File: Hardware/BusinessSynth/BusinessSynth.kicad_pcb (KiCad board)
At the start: 2 copper layers, 96 x 55 mm, 71 parts, among them J1 StylusKey, J2 StylusKey, J3 StylusKey, J4 StylusKey, J5 StylusKey, J6 StylusKey, J7 StylusKey, J8 StylusKey, J9 StylusKey, Q1 Q_PNP_BEC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

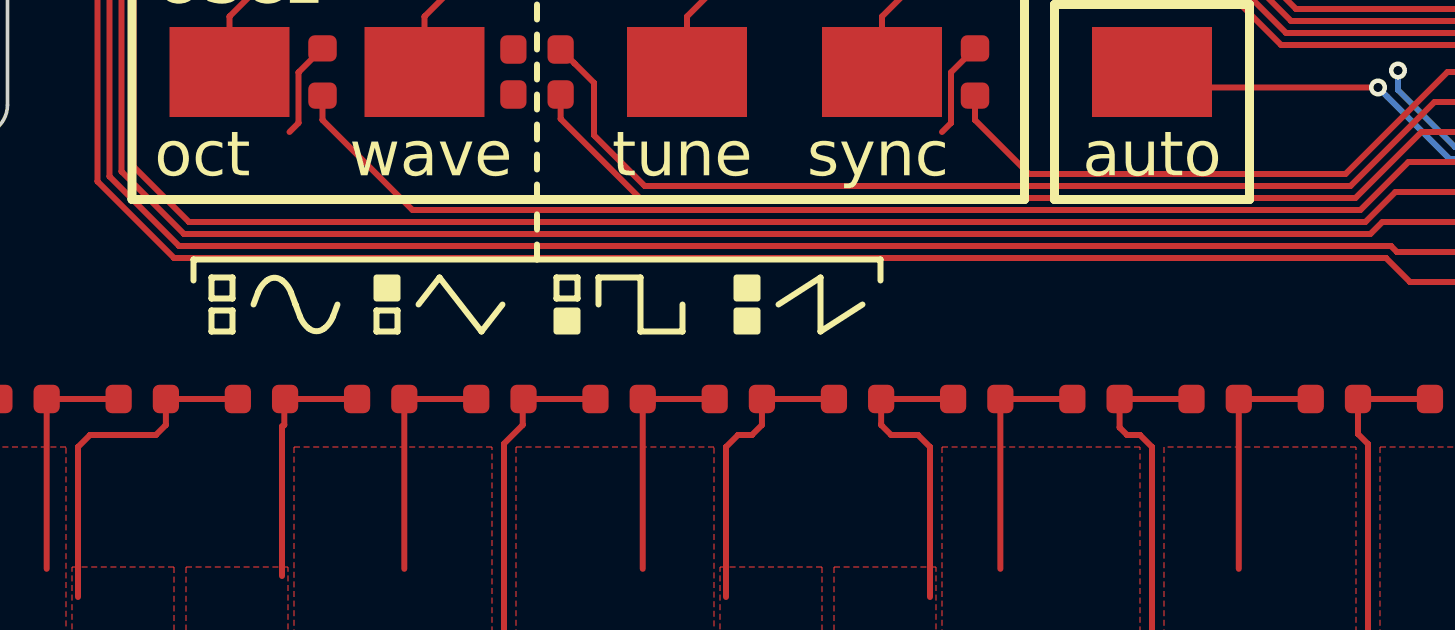
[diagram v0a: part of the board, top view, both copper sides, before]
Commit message: Add glide functionality to oscillator
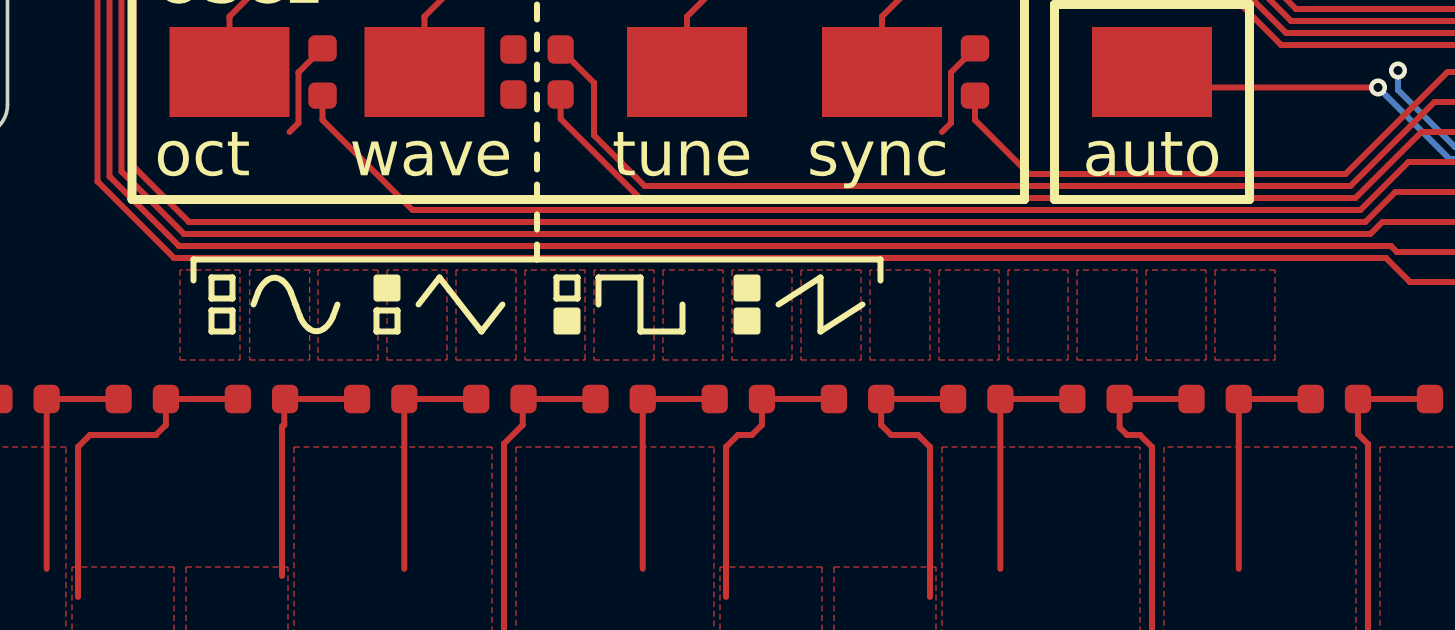
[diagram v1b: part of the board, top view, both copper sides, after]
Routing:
- added copper zone on F.Cu, net (none)
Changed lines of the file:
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@@
-(kicad_pcb (version 20171130) (host pcbnew "(5.1.0)-1")
+(kicad_pcb (version 20171130) (host pcbnew "(5.1.2)-2")
   (general
     (thickness 0.6)
-    (drawings 127)
+    (drawings 128)
     (tracks 352)
     (zones 0)
@@
   (layers
     (0 F.Cu signal)
-    (31 B.Cu signal)
-    (32 B.Adhes user)
-    (33 F.Adhes user)
-    (34 B.Paste user)
-    (35 F.Paste user)
-    (36 B.SilkS user)
-    (37 F.SilkS user)
-    (38 B.Mask user)
+    (31 B.Cu signal hide)
+    (32 B.Adhes user hide)
+    (33 F.Adhes user hide)
+    (34 B.Paste user hide)
+    (35 F.Paste user hide)
+    (36 B.SilkS user hide)
+    (37 F.SilkS user hide)
+    (38 B.Mask user hide)
     (39 F.Mask user)
-    (40 Dwgs.User user)
-    (41 Cmts.User user)
-    (42 Eco1.User user)
-    (43 Eco2.User user)
-    (44 Edge.Cuts user)
-    (45 Margin user)
+    (40 Dwgs.User user hide)
+    (41 Cmts.User user hide)
+    (42 Eco1.User user hide)
+    (43 Eco2.User user hide)
+    (44 Edge.Cuts user hide)
+    (45 Margin user hide)
     (46 B.CrtYd user hide)
     (47 F.CrtYd user hide)
@@
       (net 1 GND) (zone_connect 1) (thermal_gap 0.3))
   )
+  (dimension 3.001666 (width 0.12) (layer F.SilkS)
+    (gr_text "3.002 mm" (at 139.077487 96.545751 -88.09084757) (layer F.SilkS)
+      (effects (font (size 1 1) (thickness 0.15)))
+    )
+    (feature1 (pts (xy 140.4 95) (xy 139.710687 95.022977)))
+    (feature2 (pts (xy 140.5 98) (xy 139.810687 98.022977)))
+    (crossbar (pts (xy 140.396782 98.003441) (xy 140.296782 95.003441)))
+    (arrow1a (pts (xy 140.296782 95.003441) (xy 140.920407 96.109783)))
+    (arrow1b (pts (xy 140.296782 95.003441) (xy 139.748216 96.148856)))
+    (arrow2a (pts (xy 140.396782 98.003441) (xy 140.945348 96.858026)))
+    (arrow2b (pts (xy 140.396782 98.003441) (xy 139.773157 96.897099)))
+  )
   (gr_line (start 132.35 104.45) (end 131.65 104.45) (layer F.SilkS) (width 0.2))
   (gr_line (start 131.65 105.15) (end 132.35 105.15) (layer F.SilkS) (width 0.2))
@@
   (gr_line (start 102 125) (end 188 125) (layer Edge.Cuts) (width 0.15))
   (gr_line (start 100 72) (end 100 123) (layer Edge.Cuts) (width 0.15))
-  (via (at 178.262742 84.5) (size 0.8) (drill 0.4) (layers F.Cu B.Cu) (net 30))
-  (segment (start 179.38873 83.374012) (end 178.262742 84.5) (width 0.5) (layer B.Cu) (net 30))
   (via (at 193.5 120.75) (size 0.6) (drill 0.3) (layers F.Cu B.Cu) (net 1))
   (via (at 103.25 107.4) (size 0.6) (drill 0.3) (layers F.Cu B.Cu) (net 1))
@@
   (segment (start 169.535 88.465) (end 169 88.465) (width 0.2) (layer F.Cu) (net 29))
   (segment (start 169.735 88.265) (end 169.535 88.465) (width 0.2) (layer F.Cu) (net 29))
+  (via (at 178.262742 84.5) (size 0.8) (drill 0.4) (layers F.Cu B.Cu) (net 30))
+  (segment (start 179.38873 83.374012) (end 178.262742 84.5) (width 0.5) (layer B.Cu) (net 30))
   (segment (start 178.262742 86.827258) (end 178.262742 84.5) (width 0.5) (layer F.Cu) (net 30))
   (segment (start 176.2875 87.345) (end 177.745 87.345) (width 0.5) (layer F.Cu) (net 30))
@@
       )
     )
+  )
+  (zone (net 0) (net_name "") (layer F.Cu) (hatch edge 0.508)
+    (priority 1)
+    (connect_pads (clearance 0.2))
+    (min_thickness 0.254)
+    (fill yes (arc_segments 32) (thermal_gap 0.508) (thermal_bridge_width 0.508))
+    (polygon
+      (pts
+        (xy 130.6 106.1) (xy 132.6 106.1) (xy 132.6 103.1) (xy 130.6 103.1)
+      )
+    )
+  )
+  (zone (net 0) (net_name "") (layer F.Cu) (hatch edge 0.508)
+    (priority 1)
+    (connect_pads (clearance 0.2))
+    (min_thickness 0.254)
+    (fill yes (arc_segments 32) (thermal_gap 0.508) (thermal_bridge_width 0.508))
+    (polygon
+      (pts
+        (xy 132.920796 106.1) (xy 134.920796 106.1) (xy 134.920796 103.1) (xy 132.920796 103.1)
+      )
+    )
+  )
+  (zone (net 0) (net_name "") (layer F.Cu) (hatch edge 0.508)
+    (priority 1)
+    (connect_pads (clearance 0.2))
+    (min_thickness 0.254)
+    (fill yes (arc_segments 32) (thermal_gap 0.508) (thermal_bridge_width 0.508))
+    (polygon
+      (pts
+        (xy 135.2 106.1) (xy 137.2 106.1) (xy 137.2 103.1) (xy 135.2 103.1)
+      )
+    )
+  )
+  (zone (net 0) (net_name "") (layer F.Cu) (hatch edge 0.508)
+    (priority 1)
+    (connect_pads (clearance 0.2))
+    (min_thickness 0.254)
+    (fill yes (arc_segments 32) (thermal_gap 0.508) (thermal_bridge_width 0.508))
+    (polygon
+      (pts
+        (xy 137.5 106.1) (xy 139.5 106.1) (xy 139.5 103.1) (xy 137.5 103.1)
+      )
+    )
+  )
+  (zone (net 0) (net_name "") (layer F.Cu) (hatch edge 0.508)
+    (priority 1)
+    (connect_pads (clearance 0.2))
+    (min_thickness 0.254)
+    (fill yes (arc_segments 32) (thermal_gap 0.508) (thermal_bridge_width 0.508))
+    (polygon
+      (pts
+        (xy 139.8 106.1) (xy 141.8 106.1) (xy 141.8 103.1) (xy 139.8 103.1)
+      )
+    )
+  )
+  (zone (net 0) (net_name "") (layer F.Cu) (hatch edge 0.508)
+    (priority 1)
+    (connect_pads (clearance 0.2))
+    (min_thickness 0.254)
+    (fill yes (arc_segments 32) (thermal_gap 0.508) (thermal_bridge_width 0.508))
+    (polygon
+      (pts
+        (xy 142.1 106.1) (xy 144.1 106.1) (xy 144.1 103.1) (xy 142.1 103.1)
+      )
+    )
+  )
+  (zone (net 0) (net_name "") (layer F.Cu) (hatch edge 0.508)
+    (priority 1)
+    (connect_pads (clearance 0.2))
+    (min_thickness 0.254)
+    (fill yes (arc_segments 32) (thermal_gap 0.508) (thermal_bridge_width 0.508))
+    (polygon
+      (pts
+        (xy 144.4 106.1) (xy 146.4 106.1) (xy 146.4 103.1) (xy 144.4 103.1)
+      )
+    )
+  )
+  (zone (net 0) (net_name "") (layer F.Cu) (hatch edge 0.508)
+    (priority 1)
+    (connect_pads (clearance 0.2))
+    (min_thickness 0.254)
+    (fill yes (arc_segments 32) (thermal_gap 0.508) (thermal_bridge_width 0.508))
+    (polygon
+      (pts
+        (xy 146.7 106.1) (xy 148.7 106.1) (xy 148.7 103.1) (xy 146.7 103.1)
+      )
+    )
+  )
+  (zone (net 0) (net_name "") (layer F.Cu) (hatch edge 0.508)
+    (priority 1)
+    (connect_pads (clearance 0.2))
+    (min_thickness 0.254)
+    (fill yes (arc_segments 32) (thermal_gap 0.508) (thermal_bridge_width 0.508))
+    (polygon
+      (pts
+        (xy 149 106.1) (xy 151 106.1) (xy 151 103.1) (xy 149 103.1)
+      )
+    )
+  )
+  (zone (net 0) (net_name "") (layer F.Cu) (hatch edge 0.508)
+    (priority 1)
+    (connect_pads (clearance 0.2))
+    (min_thickness 0.254)
+    (fill yes (arc_segments 32) (thermal_gap 0.508) (thermal_bridge_width 0.508))
+    (polygon
+      (pts
+        (xy 151.3 106.1) (xy 153.3 106.1) (xy 153.3 103.1) (xy 151.3 103.1)
+      )
+    )
+  )
+  (zone (net 0) (net_name "") (layer F.Cu) (hatch edge 0.508)
+    (priority 1)
+    (connect_pads (clearance 0.2))
+    (min_thickness 0.254)
+    (fill yes (arc_segments 32) (thermal_gap 0.508) (thermal_bridge_width 0.508))
+    (polygon
+      (pts
+        (xy 162.8 106.1) (xy 164.8 106.1) (xy 164.8 103.1) (xy 162.8 103.1)
+      )
+    )
+  )
+  (zone (net 0) (net_name "") (layer F.Cu) (hatch edge 0.508)
+    (priority 1)
+    (connect_pads (clearance 0.2))
+    (min_thickness 0.254)
+    (fill yes (arc_segments 32) (thermal_gap 0.508) (thermal_bridge_width 0.508))
+    (polygon
+      (pts
+        (xy 155.9 106.1) (xy 157.9 106.1) (xy 157.9 103.1) (xy 155.9 103.1)
+      )
+    )
+  )
+  (zone (net 0) (net_name "") (layer F.Cu) (hatch edge 0.508)
+    (priority 1)
+    (connect_pads (clearance 0.2))
+    (min_thickness 0.254)
+    (fill yes (arc_segments 32) (thermal_gap 0.508) (thermal_bridge_width 0.508))
+    (polygon
+      (pts
+        (xy 153.6 106.1) (xy 155.6 106.1) (xy 155.6 103.1) (xy 153.6 103.1)
+      )
+    )
+  )
+  (zone (net 0) (net_name "") (layer F.Cu) (hatch edge 0.508)
+    (priority 1)
+    (connect_pads (clearance 0.2))
+    (min_thickness 0.254)
+    (fill yes (arc_segments 32) (thermal_gap 0.508) (thermal_bridge_width 0.508))
+    (polygon
+      (pts
+        (xy 165.1 106.1) (xy 167.1 106.1) (xy 167.1 103.1) (xy 165.1 103.1)
+      )
+    )
+  )
+  (zone (net 0) (net_name "") (layer F.Cu) (hatch edge 0.508)
+    (priority 1)
+    (connect_pads (clearance 0.2))
+    (min_thickness 0.254)
+    (fill yes (arc_segments 32) (thermal_gap 0.508) (thermal_bridge_width 0.508))
+    (polygon
+      (pts
+        (xy 160.5 106.1) (xy 162.5 106.1) (xy 162.5 103.1) (xy 160.5 103.1)
+      )
+    )
+  )
+  (zone (net 0) (net_name "") (layer F.Cu) (hatch edge 0.508)
+    (priority 1)
+    (connect_pads (clearance 0.2))
+    (min_thickness 0.254)
+    (fill yes (arc_segments 32) (thermal_gap 0.508) (thermal_bridge_width 0.508))
+    (polygon
+      (pts
+        (xy 158.2 106.1) (xy 160.2 106.1) (xy 160.2 103.1) (xy 158.2 103.1)
+      )
+    )
+  )
+  (zone (net 0) (net_name "") (layer F.Mask) (hatch edge 0.508)
+    (connect_pads (clearance 0.15))
+    (min_thickness 0.254)
+    (fill yes (arc_segments 32) (thermal_gap 0.508) (thermal_bridge_width 0.508))
+    (polygon
+      (pts
+        (xy 130.6 103.1) (xy 130.6 106.1) (xy 167.1 106.1) (xy 167.1 103.1)
+      )
+    )

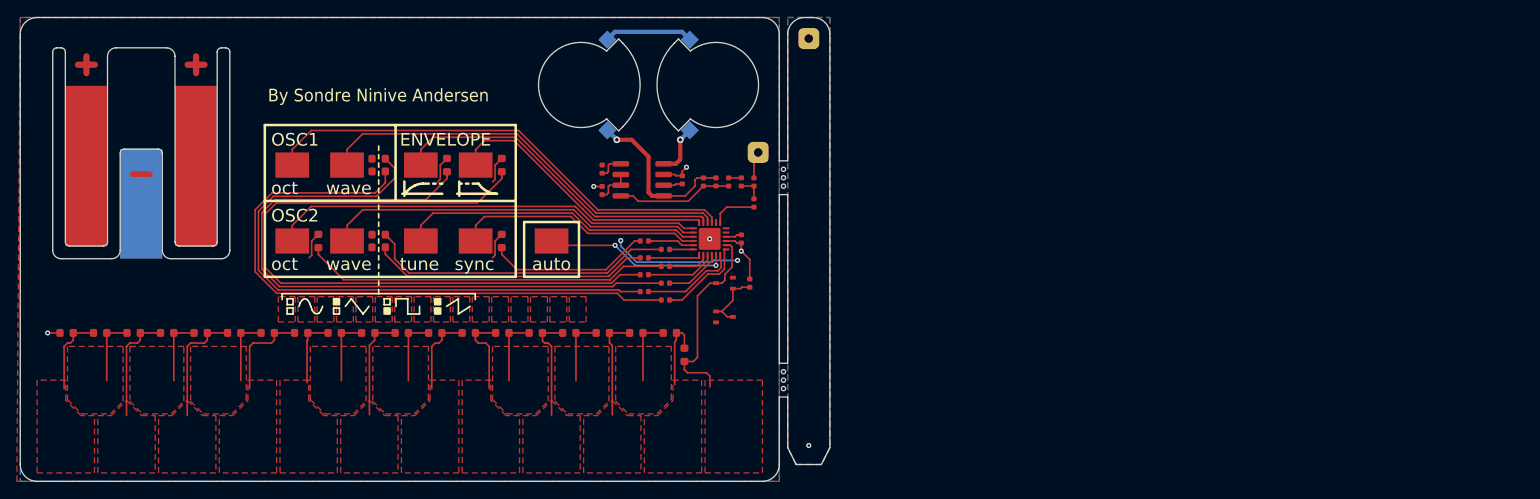
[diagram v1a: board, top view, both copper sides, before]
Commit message: Start layout of new patch-panel
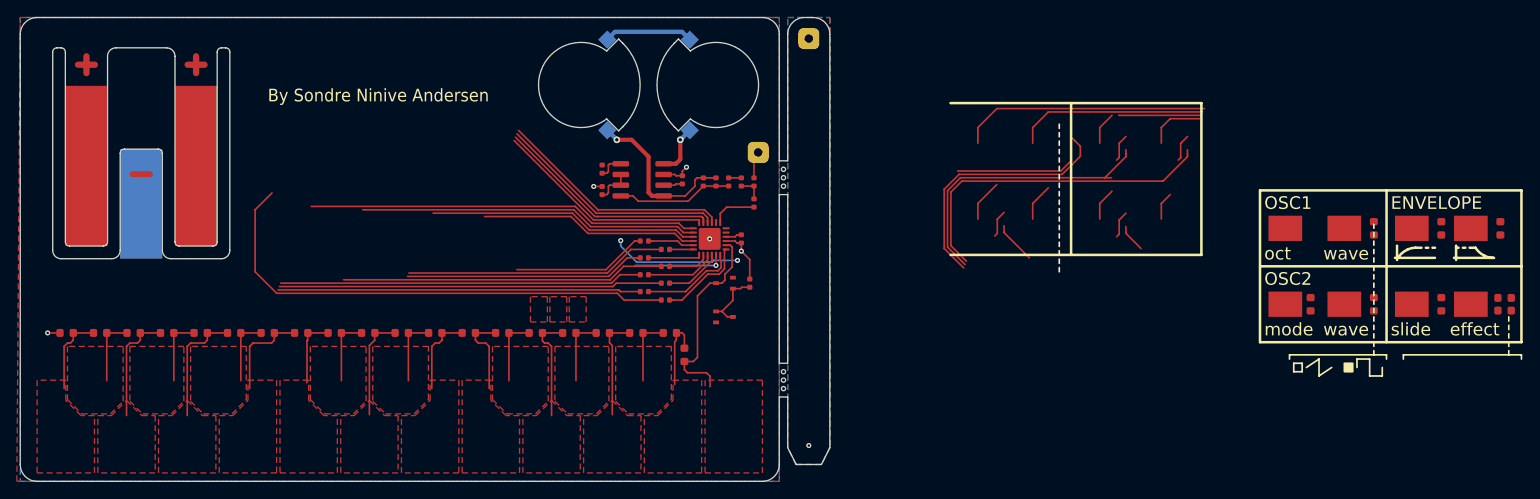
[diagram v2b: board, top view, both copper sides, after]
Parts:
- removed J1: StylusKey, BusinessSynth:StylusKey
- moved D8 134.3 mm to (276.0, 103.2)
- moved D3 133.7 mm to (276.0, 104.8)
- moved D5 118.6 mm to (275.5, 95.0)
- moved J4 118.5 mm to (257.0, 104.0)
- moved J8 118.5 mm to (257.0, 95.0)
- moved D2 118.3 mm to (260.5, 104.0), turned to 270 degrees
- moved D7 118.3 mm to (260.5, 95.0), turned to 270 degrees
- moved J2 118.2 mm to (272.0, 104.0)
- moved J6 118.2 mm to (272.0, 95.0)
- moved D6 118.1 mm to (268.5, 95.0)
- moved J5 118.0 mm to (250.0, 104.0)
- moved J9 118.0 mm to (250.0, 95.0)
- moved D4 117.9 mm to (253.0, 104.0)
- moved J3 117.7 mm to (265.0, 104.0)
- moved J7 117.7 mm to (265.0, 95.0)
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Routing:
- net Net-(J1-Pad1): track 21.4 -> 10.8 mm, vias 2 -> 1
- net Net-(D2-Pad1): track 36.8 -> 31.1 mm
- net Net-(D3-Pad1): track 33.0 -> 28.5 mm
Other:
- board text added: "effect"
- board text added: "mode"
- board text added: "slide"
- board text removed: "auto"
- board text removed: "sync"
- board text removed: "tune"

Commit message: Fix speaker-driver footprint, and complete new routing
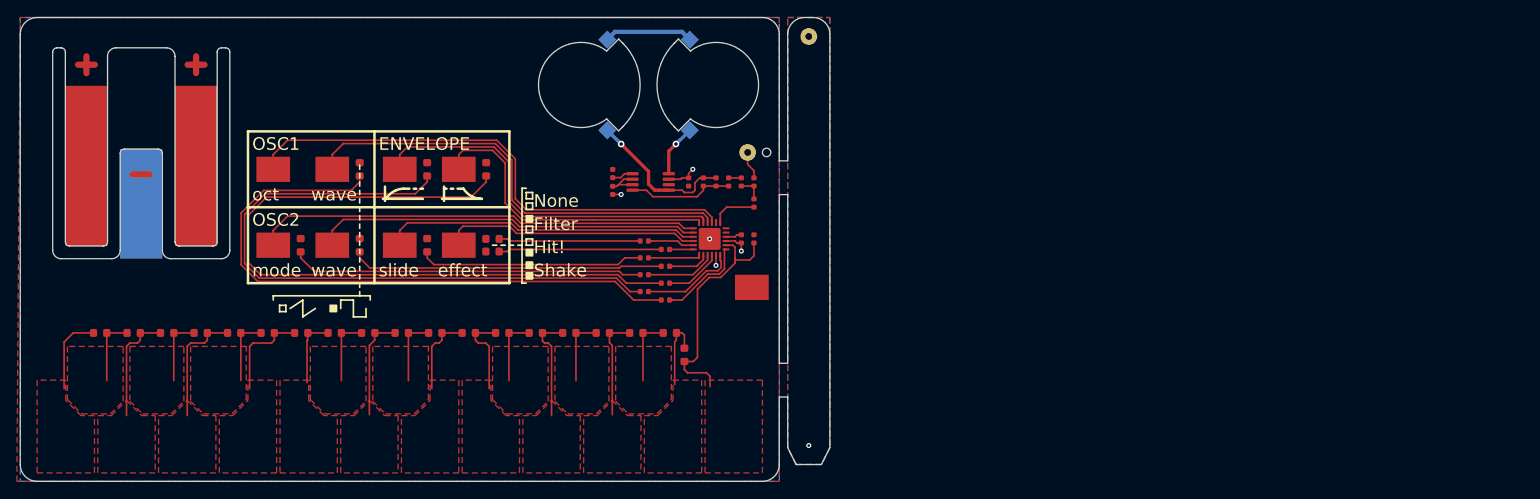
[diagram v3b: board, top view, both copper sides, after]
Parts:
- removed Q1, Q2: Q_PNP_BEC, BusinessSynth:SOT-323_SC-70_nosilk
- removed R20: 100R, BusinessSynth:R_0603_1608Metric_nosilk
- removed REF** (x6): MountingHole_2mm, MountingHole:MountingHole_2mm
- removed Stylus (x2): SolderWirePad_single_1mmDrill, Wire_Pads:SolderWirePad_single_1mmDrill
- added H1: Stylus, Connector_Wire:SolderWirePad_1x01_Drill0.8mm, F.Cu at (193.5, 72.2)
- added H2: Stylus, Connector_Wire:SolderWirePad_1x01_Drill0.8mm, F.Cu at (186.2, 86.0)
- added H3: Strain relief, MountingHole:MountingHole_2.1mm, F.Cu at (188.5, 86.0)
- added J1: StylusKey, BusinessSynth:StylusKey, F.Cu at (186.8, 102.0)
- R1, R2, R3, R4: value 100R -> 680R
- R10, R11: value 100R -> 2K2
- R12, R13: value 100R -> 3K3
- R14, R15: value 100R -> 6K8
- R16: value 100R -> 10K
- R17: value 100R -> 15K
- R18: value 100R -> 33K
- R19: value 100R -> 100K
- R5, R6, R7: value 100R -> 1K
- R8, R9: value 100R -> 1K5
- U2: footprint BusinessSynth:SOP-8_3.76x4.96mm_P1.27mm_nosilk -> BusinessSynth:MSOP-8-1EP_3x3mm_P0.65mm_nosilk
- moved D5 142.3 mm to (133.2, 97.0)
- moved D8 136.6 mm to (140.2, 88.0), turned to 90 degrees
- moved D3 128.0 mm to (148.2, 97.0), turned to 90 degrees
- moved J2 120.2 mm to (152.0, 97.0)
- moved J3 120.2 mm to (145.0, 97.0)
- moved J4 120.2 mm to (137.0, 97.0)
- moved J5 120.2 mm to (130.0, 97.0)
- moved J6 120.2 mm to (152.0, 88.0)
- moved J7 120.2 mm to (145.0, 88.0)
- moved J8 120.2 mm to (137.0, 88.0)
- moved J9 120.2 mm to (130.0, 88.0)
- moved D6 113.5 mm to (155.2, 88.0)
- moved D4 113.0 mm to (140.2, 97.0)
- moved D1 112.8 mm to (156.0, 96.2), turned to 180 degrees
- moved D7 112.5 mm to (148.2, 88.0), turned to 90 degrees
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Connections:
- net /Led1 renamed Net-(R26-Pad1)
- net /Led2 renamed Net-(R27-Pad1)
- net /Led3 renamed Net-(R28-Pad1)
- net /Led4 renamed Net-(R29-Pad1)
- net /Led5 renamed Net-(R30-Pad1)
- net /Led6 renamed Net-(R31-Pad1)
- R21 pad 1: Net-(Q1-Pad1) -> VDD
- R21 pad 2: GND -> /KeyC3
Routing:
- net Net-(D5-Pad1): track 82.6 -> 41.8 mm
- net VDD: track 32.5 -> 1.91 mm, vias 2 -> 0
- net Net-(D2-Pad1): track 31.1 -> 19.3 mm
- net Net-(J1-Pad1): track 10.8 -> 1.21 mm
- net Net-(Q1-Pad1): track 7.58 -> 0.00 mm
- net Net-(D6-Pad1): track 79.5 -> 86.2 mm
- net Net-(D4-Pad1): track 43.4 -> 37.1 mm
- net GND: track 15.8 -> 10.8 mm, vias 6 -> 4
- net /KeyC3: track 23.7 -> 28.4 mm
- net Net-(J7-Pad1): track 40.4 -> 44.9 mm
- net Net-(D7-Pad1): track 73.9 -> 78.1 mm
- net Net-(J9-Pad1): track 57.4 -> 61.7 mm
- net Net-(J6-Pad1): track 32.7 -> 36.6 mm
- net Net-(J8-Pad1): track 50.1 -> 53.8 mm
- net Net-(D1-Pad1): track 19.4 -> 16.8 mm
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- added copper zone on B.Cu, net /StylusGND
- added copper zone on F.Cu, net /StylusGND
- removed copper zone on F.Cu, net (none)
- removed copper zone on F.Cu, net GND
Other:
- board text added: "Filter"
- board text added: "Hit!"
- board text added: "None"
- board text added: "Shake"
- board text removed: "By Sondre Ninive Andersen"
